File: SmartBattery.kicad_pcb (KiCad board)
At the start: 4 copper layers, 100 x 80 mm, 413 parts, among them J1 USB_C_Receptacle_USB2.0, J10 JST 2P-1.0, J11 JST 2P-1.0, J12 Conn_01x10_Male, J13 Conn_01x03_Male, J15 USB_C_Receptacle_USB2.0, J2 ST-USB-003A, J3 Barrel_Jack_MountingPin, J4 JST 2P-1.0, J5 JST 2P-1.0, J6 JST 2P-1.0, J7 JST 2P-1.0, J8 JST 2P-1.0, J9 JST 2P-1.0, Q1 VBA2625, Q10 AON7400A, Q11 AON7400A, Q12 BSC067N06LS3, Q13 BSC067N06LS3, Q14 2n7002K, Q15 VBA2625, Q16 VBA2625, Q17 VBA2625, Q18 VBA2625, Q19 VBA2625, Q2 2n7002K, Q20 VBA2625, Q21 2n7002K, Q22 AO3401A, Q23 VBA2625, Q24 VBA2625, Q25 2n7002K, Q26 VBA2625, Q27 VBA2625, Q3 AON7400A, Q4 AON7400A, Q5 AON7400A, Q6 AON7400A, Q7 2n7002K, Q8 AON7400A, Q9 AON7400A, SW1 SW_Push, SW2 SW_Push, SW3 SW_Push, SW4 SW_Push, U1 BQ25703ARSNR, U10 ESP32-WROOM-32U, U11 STUSB4500, U12 STUSB4700, U13 TPS2511DGNR, U14 HT7533-1, U15 LMR14030SDDAR, U2 BQ294706DSGR, U3 ITV4030, U4 BQ40Z50, U5 LM5175PWPR, U6 STM32F730R8T6, U7 W25Q128JVSIQ, U8 LMR14030SDDAR, U9 FS35ND01G-S1Y2QWFI000, Y1 Q13FC1350000400, Y2 Crystal_GND24

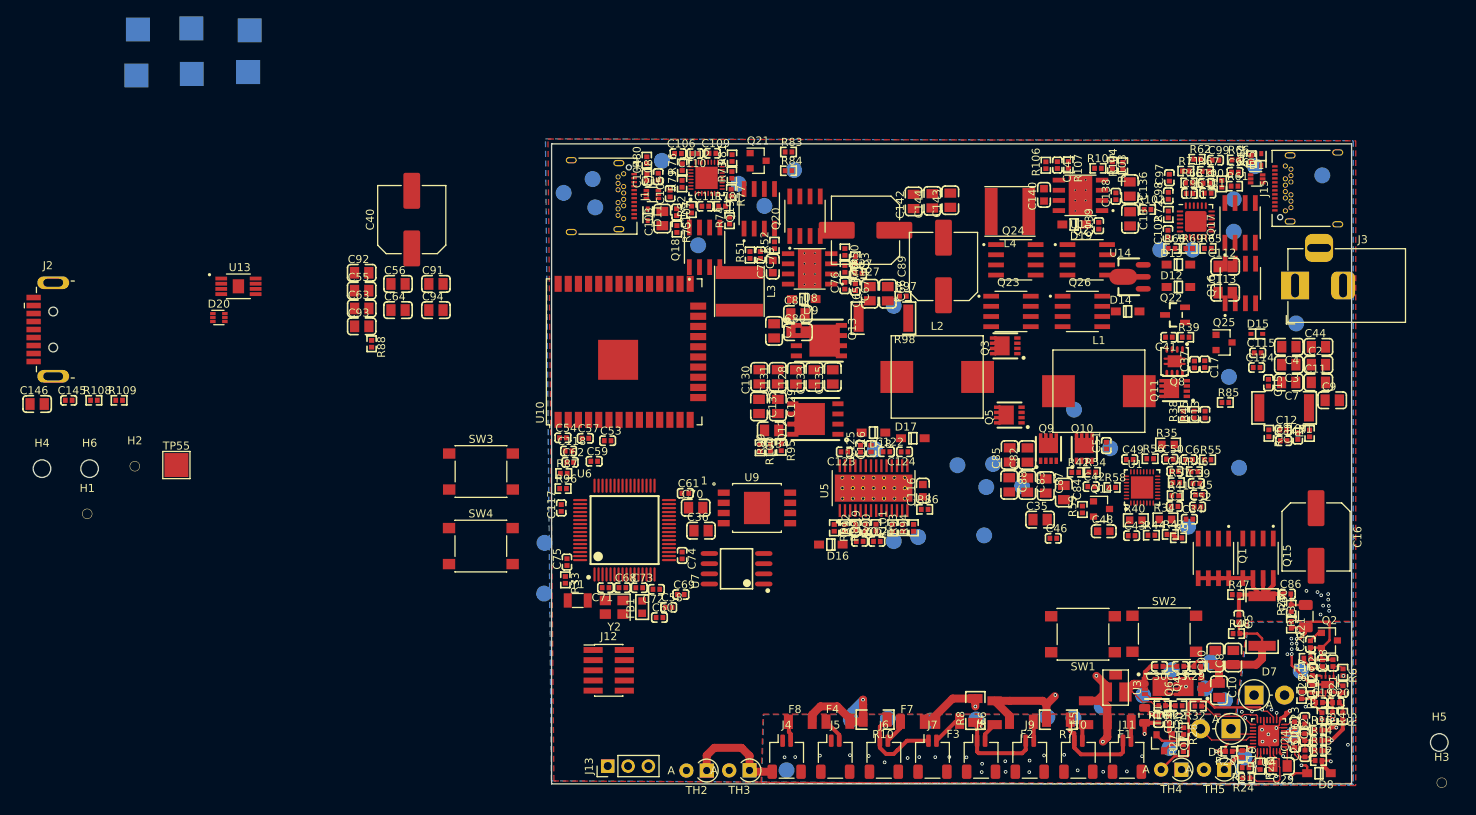
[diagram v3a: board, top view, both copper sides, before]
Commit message: Layout placed type-c + barrel jack
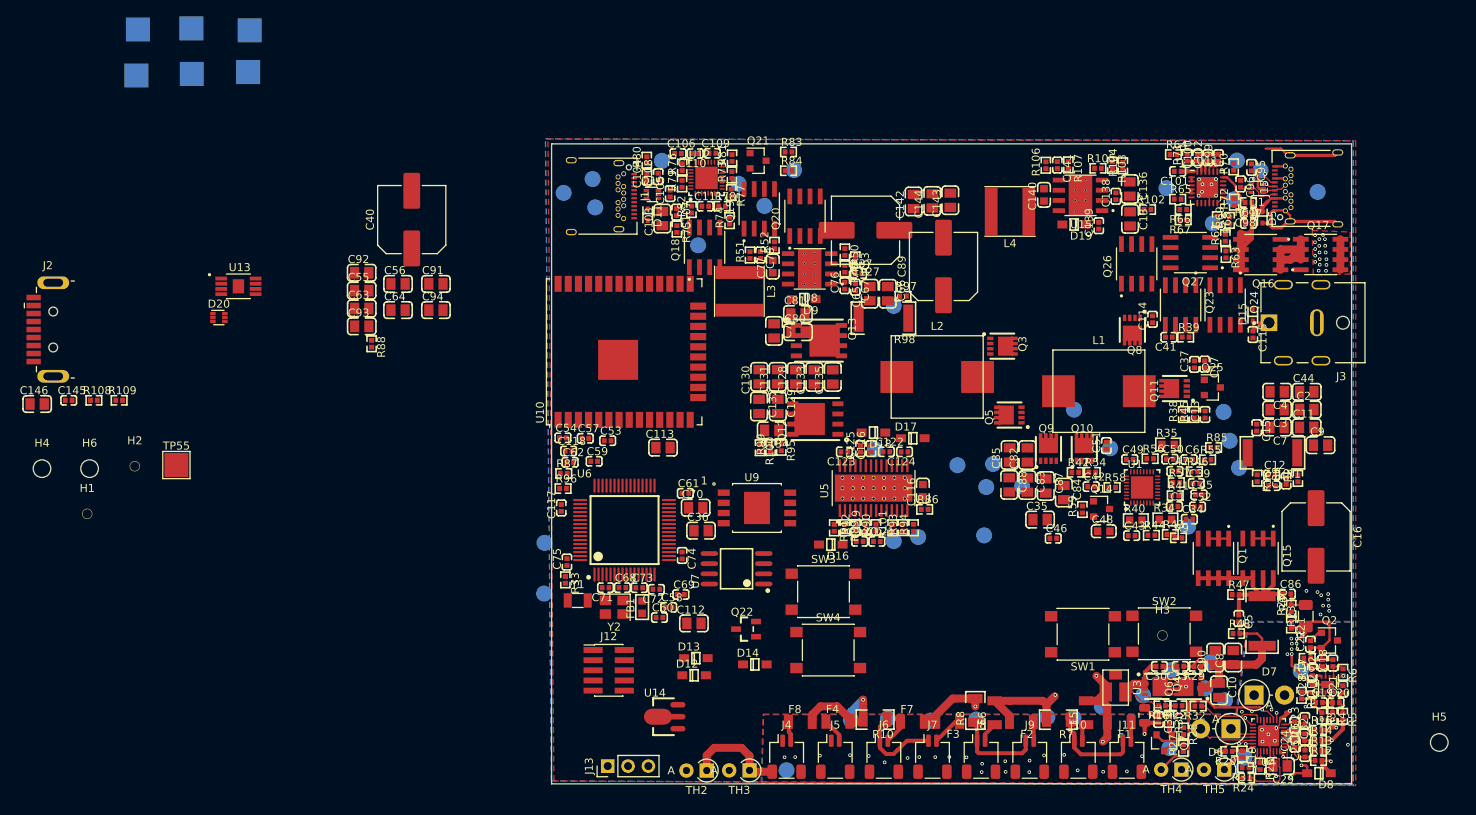
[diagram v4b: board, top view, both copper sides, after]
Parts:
- J3: value Barrel_Jack_MountingPin -> JACK-C-PC-10A-RA(R); footprint Connector_BarrelJack:BarrelJack_Horizontal -> SmartBattery:GLOBTECK_JACK-C-PC-10A-RA(R)
- Q8: value AON7400A -> AON7400A; footprint lc_lib:QFN-8_3X3X065P -> lc_lib:SON-8_3.3X3.3MM
- moved U14 80.0 mm to (15.8, 71.6)
- moved C112 80.0 mm to (17.8, 59.9)
- moved D13 77.8 mm to (18.0, 64.3)
- moved D12 77.6 mm to (17.8, 66.4)
- moved C113 72.9 mm to (13.9, 38.0)
- moved Q22 66.5 mm to (24.3, 60.7)
- moved D14 64.2 mm to (25.4, 65.1)
- moved SW3 45.4 mm to (34.0, 56.0)
- moved SW4 45.3 mm to (34.6, 63.3)
- moved H3 39.5 mm to (76.4, 61.5)
- moved Q24 26.8 mm to (84.2, 20.1), turned to 270 degrees
- moved Q23 21.2 mm to (78.6, 20.1), turned to 270 degrees
- moved TP30 21.0 mm to (95.8, 6.01)
- moved TP45 16.9 mm to (84.8, 37.1)
- moved C114 14.3 mm to (75.1, 21.9), turned to 90 degrees
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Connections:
- D1 pad 4: Net-(D1-Pad4) -> Net-(C95-Pad2)
- J15 pad B5: Net-(D1-Pad4) -> Net-(C95-Pad2)
- U11 pad 4: Net-(D1-Pad4) -> Net-(C95-Pad2)
- U11 pad 5: Net-(D1-Pad4) -> Net-(C95-Pad2)
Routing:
- net GND: track 3.20 -> 45.7 mm, vias 9 -> 16
- net Net-(C101-Pad1): track 0.00 -> 30.9 mm
- net Net-(C95-Pad2): track 0.00 -> 15.6 mm, vias 0 -> 1
- net Net-(D7-Pad2): track 0.00 -> 11.4 mm, vias 0 -> 1
- net Net-(Q16-Pad1): track 0.00 -> 10.7 mm
- net Net-(D6-Pad2): track 7.29 -> 16.2 mm
- net /Barrel_Jack_Input/BARREL_RAW: track 0.00 -> 5.82 mm
- net Net-(C96-Pad2): track 0.00 -> 5.53 mm
- net /Charger/VSYS: track 0.00 -> 5.08 mm
- net /type_c_input/INPUT_DM: track 0.00 -> 4.75 mm, vias 0 -> 1
- net Net-(R61-Pad2): track 0.00 -> 4.59 mm
- net /Charger/ADAPTER_IN: track 0.00 -> 3.81 mm, vias 0 -> 18
- net /type_c_input/INPUT_DP: track 0.00 -> 3.16 mm
- net /type_c_input/2v7_local: track 0.00 -> 2.81 mm
- net Net-(R72-Pad2): track 0.00 -> 2.47 mm
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- added copper zone on F.Cu, net /Charger/ADAPTER_IN
- added copper zone on In2.Cu, net /Charger/ADAPTER_IN

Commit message: Much layout wow.
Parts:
- added C147: 220u, Capacitor_SMD:C_Elec_8x10.2, F.Cu at (57.4, 16.2)
- added C148: 220u, Capacitor_SMD:C_Elec_8x10.2, F.Cu at (43.3, 13.3)
- added C149: 220u, Capacitor_SMD:C_Elec_8x10.2, F.Cu at (37.5, 37.8)
- added C150: 22u, lc_lib:0805_C, F.Cu at (45.2, 19.6)
- added C151: 22u, lc_lib:0805_C, F.Cu at (42.9, 19.6)
- added C152: 22u, lc_lib:0805_C, F.Cu at (49.6, 19.4)
- added C153: 22u, lc_lib:0805_C, F.Cu at (55.2, 24.3)
- added C154: 22u, lc_lib:0805_C, F.Cu at (57.4, 24.3)
- added D2: LED_BARG, LED_THT:LED_D5.0mm-4_RGB_Wide_Pins, F.Cu at (29.7, 37.5)
- added D3: LED_BARG, LED_THT:LED_D5.0mm-4_RGB_Wide_Pins, F.Cu at (22.4, 67.3)
- added D4: LED_BARG, LED_THT:LED_D5.0mm-4_RGB_Wide_Pins, F.Cu at (29.7, 46.5)
- added R110: 100k, lc_lib:0402_R, F.Cu at (20.1, 70.9)
- added R111: 100k, lc_lib:0402_R, F.Cu at (4.12, 67.0)
- added R112: 100k, lc_lib:0402_R, F.Cu at (1.04, 58.0)
- added R113: 100k, lc_lib:0402_R, F.Cu at (2.81, 44.8)
- added TP56: TestPoint, TestPoint:TestPoint_Pad_D2.0mm, B.Cu at (7.25, 72.7)
- added TP57: TestPoint, TestPoint:TestPoint_Pad_D2.0mm, B.Cu at (11.3, 72.7)
- added TP58: TestPoint, TestPoint:TestPoint_Pad_D2.0mm, B.Cu at (7.25, 68.7)
- added TP59: TestPoint, TestPoint:TestPoint_Pad_D2.0mm, B.Cu at (11.3, 68.7)
- added TP60: TestPoint, TestPoint:TestPoint_Pad_D2.0mm, B.Cu at (9.96, 77.7)
- J12: value Conn_01x10_Male -> Conn_02x05_Odd_Even
- TP55: moved to B.Cu
- U7: value W25Q128JVSIQ -> LY68L6400SLIT; footprint lc_lib:SOP-8_208MIL -> lc_lib:SOP-8_150MIL
- moved C40 119.6 mm to (95.6, 48.4), turned to 270 degrees
- moved C145 116.6 mm to (53.1, 5.46), turned to 270 degrees
- moved R109 108.9 mm to (52.8, 11.1)
- moved J2 108.5 mm to (43.7, 3.29), turned to 90 degrees
- moved C146 107.4 mm to (40.2, 7.68), turned to 180 degrees
- moved R108 106.8 mm to (46.8, 7.58), turned to 90 degrees
- moved U13 90.3 mm to (50.7, 8.31), turned to 180 degrees
- moved D20 86.7 mm to (44.1, 8.44), turned to 270 degrees
- moved C55 86.7 mm to (54.8, 55.2), turned to 270 degrees
- moved C92 86.1 mm to (54.7, 51.5), turned to 90 degrees
- moved C64 83.6 mm to (57.0, 55.2), turned to 270 degrees
- moved C56 83.4 mm to (57.0, 51.5), turned to 90 degrees
- moved R63 83.0 mm to (16.3, 61.3), turned to 0 degrees
- moved C93 82.8 mm to (51.6, 57.2)
- moved R88 82.8 mm to (52.9, 59.4)
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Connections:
- net /MCU/QUADSPI_BK2_NCS renamed Net-(U6-Pad52)
- net /type_c_input/INPUT_TYPEC_VBUS_DIV7 renamed Net-(R62-Pad1)
- net Net-(U10-Pad25) renamed /MCU/ESP32_SERIAL_BL
- net Net-(U10-Pad26) renamed /MCU/ESP32_WAKE
- net Net-(U10-Pad33) renamed /MCU/ESP32_SDA
- net Net-(U10-Pad34) renamed /MCU/ESP32_UART_RX
- net Net-(U10-Pad35) renamed /MCU/ESP32_UART_TX
- net Net-(U10-Pad36) renamed /MCU/ESP32_SCL
- net Net-(U6-Pad10) renamed /MCU/ADC1_IN12
- net Net-(U6-Pad11) renamed /MCU/ADC1_IN13
- net Net-(U6-Pad20) renamed /MCU/DAC1
- net Net-(U6-Pad21) renamed /MCU/DAC2
- net Net-(U6-Pad24) renamed /MCU/ADC1_IN14
- net Net-(U6-Pad28) renamed /MCU/I2C2_SCL
- net Net-(U6-Pad29) renamed /MCU/I2C2_SDA
- net Net-(U6-Pad44) renamed /MCU/USB_FS_DM
- net Net-(U6-Pad45) renamed /MCU/USB_FS_DP
- net Net-(U6-Pad53) renamed /MCU/UART5_TX
- net Net-(U6-Pad54) renamed /MCU/UART5_RX
- net Net-(U6-Pad57) renamed /MCU/I2C1_SMBA
- net Net-(U6-Pad59) renamed /MCU/I2C1_SDA
- net Net-(U6-Pad61) renamed /MCU/I2C1_SCL
- net Net-(U6-Pad8) renamed /MCU/ADC1_IN10
- net Net-(U6-Pad9) renamed /MCU/ADC1_IN11
- C101 pad 1: Net-(C101-Pad1) -> /type_c_input/INPUT_TYPEC_VBUS_RAW
- C112 pad 1: Net-(C112-Pad1) -> GND
- C113 pad 1: Net-(C113-Pad1) -> GND
- C127 pad 1: GND -> /Type_C_Output/OUTPUT_TYPEC_PWR
- C127 pad 2: /Type_C_Output/OUTPUT_TYPEC_PWR -> GND
- C36 pad 2: /Peripheral_3p3v/3p3v -> +3.3VP
- C40 pad 1: GND -> /Charger/VSYS
- C40 pad 2: /Charger/VSYS -> GND
- C53 pad 1: /Peripheral_3p3v/3p3v -> +3.3VP
- C54 pad 1: /Peripheral_3p3v/3p3v -> +3.3VP
- C57 pad 1: /Peripheral_3p3v/3p3v -> +3.3VP
- C59 pad 1: /Peripheral_3p3v/3p3v -> +3.3VP
- C61 pad 1: /Peripheral_3p3v/3p3v -> +3.3VP
- C62 pad 1: /Peripheral_3p3v/3p3v -> +3.3VP
- C74 pad 1: /Peripheral_3p3v/3p3v -> +3.3VP
- C75 pad 1: /Peripheral_3p3v/3p3v -> +3.3VP
- C97 pad 2: Net-(C101-Pad1) -> /type_c_input/INPUT_TYPEC_VBUS_RAW
- C98 pad 1: Net-(C101-Pad1) -> /type_c_input/INPUT_TYPEC_VBUS_RAW
- D12 pad 1: Net-(D12-Pad1) -> Net-(C112-Pad2)
- D12 pad 2: Net-(D12-Pad2) -> /Barrel_Jack_Input/BARREL_RAW
- D13 pad 1: Net-(D13-Pad1) -> +3.3VP
- D13 pad 2: Net-(D13-Pad2) -> Net-(C113-Pad2)
- D14 pad 1: Net-(D14-Pad1) -> Net-(C112-Pad2)
- D14 pad 2: Net-(D14-Pad2) -> /type_c_input/INPUT_TYPEC_VBUS_RAW
- D5 pad 2: Net-(C101-Pad1) -> /type_c_input/INPUT_TYPEC_VBUS_RAW
- FB1 pad 1: /Peripheral_3p3v/3p3v -> +3.3VP
- J12 pad 1: Net-(J12-Pad1) -> +3.3VP
- J12 pad 10: Net-(J12-Pad10) -> /MCU/NRST
- J12 pad 2: Net-(J12-Pad2) -> /MCU/SWDIO
- J12 pad 3: Net-(J12-Pad3) -> GND
- J12 pad 4: Net-(J12-Pad4) -> /MCU/SWDCLK
- J12 pad 5: Net-(J12-Pad5) -> GND
- J12 pad 6: Net-(J12-Pad6) -> /MCU/SWO
- J15 pad A4: Net-(C101-Pad1) -> /type_c_input/INPUT_TYPEC_VBUS_RAW
- J15 pad A9: Net-(C101-Pad1) -> /type_c_input/INPUT_TYPEC_VBUS_RAW
- J15 pad B4: Net-(C101-Pad1) -> /type_c_input/INPUT_TYPEC_VBUS_RAW
- J15 pad B9: Net-(C101-Pad1) -> /type_c_input/INPUT_TYPEC_VBUS_RAW
- Q10 pad 1: Net-(Q10-Pad1) -> GND
- Q10 pad 2: Net-(Q10-Pad1) -> GND
- Q10 pad 3: Net-(Q10-Pad1) -> GND
- Q10 pad 4: Net-(Q10-Pad4) -> Net-(C51-Pad2)
- Q12 pad 0: (no net) -> /Type_C_Output/OUTPUT_TYPEC_PWR
- Q13 pad 0: (no net) -> /OutputStage/SW2
- Q16 pad 5: Net-(C101-Pad1) -> /type_c_input/INPUT_TYPEC_VBUS_RAW
- Q16 pad 6: Net-(C101-Pad1) -> /type_c_input/INPUT_TYPEC_VBUS_RAW
- Q16 pad 7: Net-(C101-Pad1) -> /type_c_input/INPUT_TYPEC_VBUS_RAW
- Q16 pad 8: Net-(C101-Pad1) -> /type_c_input/INPUT_TYPEC_VBUS_RAW
- Q22 pad 2: Net-(Q22-Pad2) -> +3.3VP
- Q22 pad 3: Net-(Q22-Pad3) -> /Peripheral_3p3v/3p3v
- R33 pad 1: /Peripheral_3p3v/3p3v -> +3.3VP
- R61 pad 1: Net-(C101-Pad1) -> /type_c_input/INPUT_TYPEC_VBUS_RAW
- R63 pad 2: Net-(C101-Pad1) -> Net-(R63-Pad2)
- SW3 pad 1: Net-(SW3-Pad1) -> /MCU/NRST
- SW3 pad 2: Net-(SW3-Pad2) -> GND
- SW4 pad 1: Net-(SW4-Pad1) -> /MCU/BOOT
- SW4 pad 2: Net-(SW4-Pad2) -> +3.3VP
- TP31 pad 1: Net-(C101-Pad1) -> /type_c_input/INPUT_TYPEC_VBUS_RAW
- U10 pad 2: Net-(U10-Pad2) -> +3.3VP
- U10 pad 3: Net-(U10-Pad3) -> /MCU/GPIO_ENABLE_ESP32
- U11 pad 24: Net-(C101-Pad1) -> /type_c_input/INPUT_TYPEC_VBUS_RAW
- U14 pad 1: Net-(U14-Pad1) -> GND
- U14 pad 2: Net-(U14-Pad2) -> Net-(C112-Pad2)
- U14 pad 3: Net-(U14-Pad3) -> Net-(C113-Pad2)
- U6 pad 19: /Peripheral_3p3v/3p3v -> +3.3VP
- U6 pad 32: /Peripheral_3p3v/3p3v -> +3.3VP
- U6 pad 34: Net-(U6-Pad34) -> /MCU/SPI2_SCK
- U6 pad 35: Net-(U6-Pad35) -> /MCU/SPI2_MISO
- U6 pad 36: Net-(U6-Pad36) -> /MCU/SPI2_MOSI
- U6 pad 46: Net-(U6-Pad46) -> /MCU/SWDIO
- U6 pad 48: /Peripheral_3p3v/3p3v -> +3.3VP
- U6 pad 49: Net-(U6-Pad49) -> /MCU/SWDCLK
- U6 pad 55: Net-(U6-Pad55) -> /MCU/SWO
- U6 pad 60: Net-(U6-Pad60) -> /MCU/BOOT
- U6 pad 64: /Peripheral_3p3v/3p3v -> +3.3VP
- U6 pad 7: Net-(U6-Pad7) -> /MCU/NRST
- U7 pad 1: Net-(U7-Pad1) -> /MCU/QUASPI_BK1_NCS
- U7 pad 2: Net-(U7-Pad2) -> /MCU/QUADSPI_BK1_IO1
- U7 pad 5: Net-(U7-Pad5) -> /MCU/QUADSPI_BK1_IO0
- U7 pad 6: Net-(U7-Pad6) -> /MCU/QUADSPI_CLK
- U7 pad 8: /Peripheral_3p3v/3p3v -> +3.3VP
- U9 pad 2: Net-(U9-Pad2) -> /MCU/SPI2_MOSI
- U9 pad 5: Net-(U9-Pad5) -> /MCU/SPI2_MISO
- U9 pad 6: Net-(U9-Pad6) -> /MCU/SPI2_SCK
- U9 pad 8: /Peripheral_3p3v/3p3v -> +3.3VP
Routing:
- net /Charger/VSYS: track 5.08 -> 56.9 mm
- net /Charger/ADAPTER_IN: track 3.81 -> 43.4 mm
- net Net-(Q23-Pad1): track 0.00 -> 33.3 mm
- net /type_c_input/INPUT_TYPEC_VBUS_RAW: track 0.00 -> 32.9 mm
- net Net-(C101-Pad1): track 30.9 -> 0.00 mm
- net /Type_C_Output/OUTPUT_TYPEC_PWR: track 0.00 -> 26.0 mm
- net /Barrel_Jack_Input/BARREL_RAW: track 5.82 -> 19.5 mm
- net Net-(C15-Pad2): track 0.00 -> 10.7 mm
- net /Peripheral_3p3v/5v0_SWITCHED_NODE: track 0.00 -> 6.78 mm
- net Net-(C43-Pad1): track 0.00 -> 5.89 mm
- net /Peripheral_3p3v/VSYS_IN_5p0: track 0.00 -> 5.65 mm
- net GND: track 45.7 -> 50.6 mm, vias 16 -> 36
- net Net-(C46-Pad1): track 0.00 -> 4.09 mm
- net Net-(C140-Pad2): track 0.00 -> 1.94 mm
- net Net-(Q23-Pad4): track 0.00 -> 1.76 mm
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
